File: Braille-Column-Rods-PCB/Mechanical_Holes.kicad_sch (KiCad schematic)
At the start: 2 parts

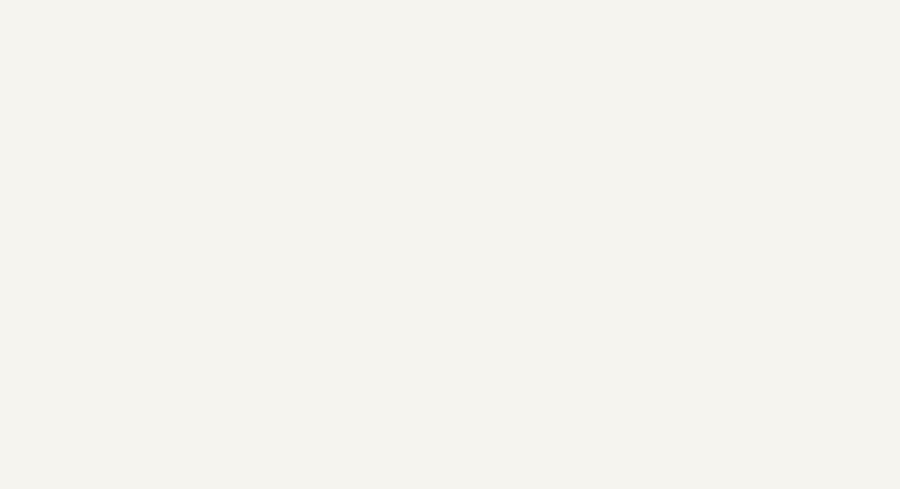
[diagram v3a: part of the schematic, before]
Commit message: Add PTHs under dots for each cell
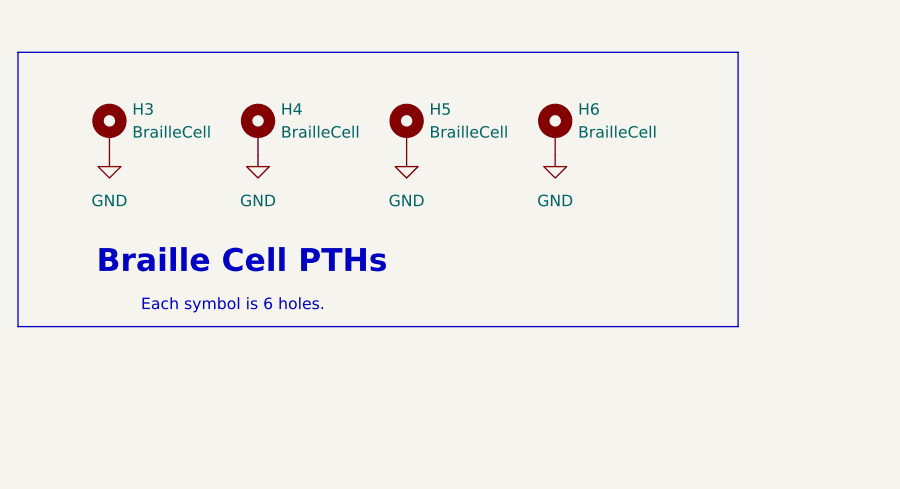
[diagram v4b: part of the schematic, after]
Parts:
- added H3, H4, H5, H6: BrailleCell, 00-lib-footprints:BrailleCell, symbol Mechanical:MountingHole_Pad
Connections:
- new net GND: H3.1, H4.1, H5.1, H6.1
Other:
- note added: "Braille Cell PTHs"
- note added: "Each symbol is 6 holes."
